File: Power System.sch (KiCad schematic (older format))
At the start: 19 parts

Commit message: changed the spliter simbole
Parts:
- removed U?: splitter, symbol splitter
- added U?: splitter, symbol splitter
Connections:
- wire segments 42 -> 44
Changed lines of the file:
@@
 	1323 4551 1848 4551
 Wire Wire Line
-	1853 4550 6700 4550
+	1853 4550 6900 4550
 Connection ~ 2400 4550
 Connection ~ 3100 4550
-$Comp
-L splitter U?
-U 1 1 59466E47
-P 1150 5075
-F 0 "U?" H 1150 4850 39  0000 C CNN
-F 1 "splitter" H 1150 5400 39  0000 C CNN
-F 2 "" H 1150 5075 39  0001 C CNN
-F 3 "" H 1150 5075 39  0001 C CNN
-	1    1150 5075
-	0    1    1    0
-$EndComp
 Wire Wire Line
 	1325 4550 1150 4550
@@
 	1    0    0    -1
 $EndComp
+$Comp
+L splitter U?
+U 1 1 594B2CCC
+P 1150 4875
+F 0 "U?" H 1190 4795 39  0000 C CNN
+F 1 "splitter" H 1180 4985 39  0000 C CNN
+F 2 "" H 1150 4875 39  0001 C CNN
+F 3 "" H 1150 4875 39  0001 C CNN
+	1    1150 4875
+	0    1    1    0
+$EndComp
+Wire Wire Line
+	1150 5375 1150 5075
+Wire Wire Line
+	7200 4550 7300 4550
 $EndSCHEMATC

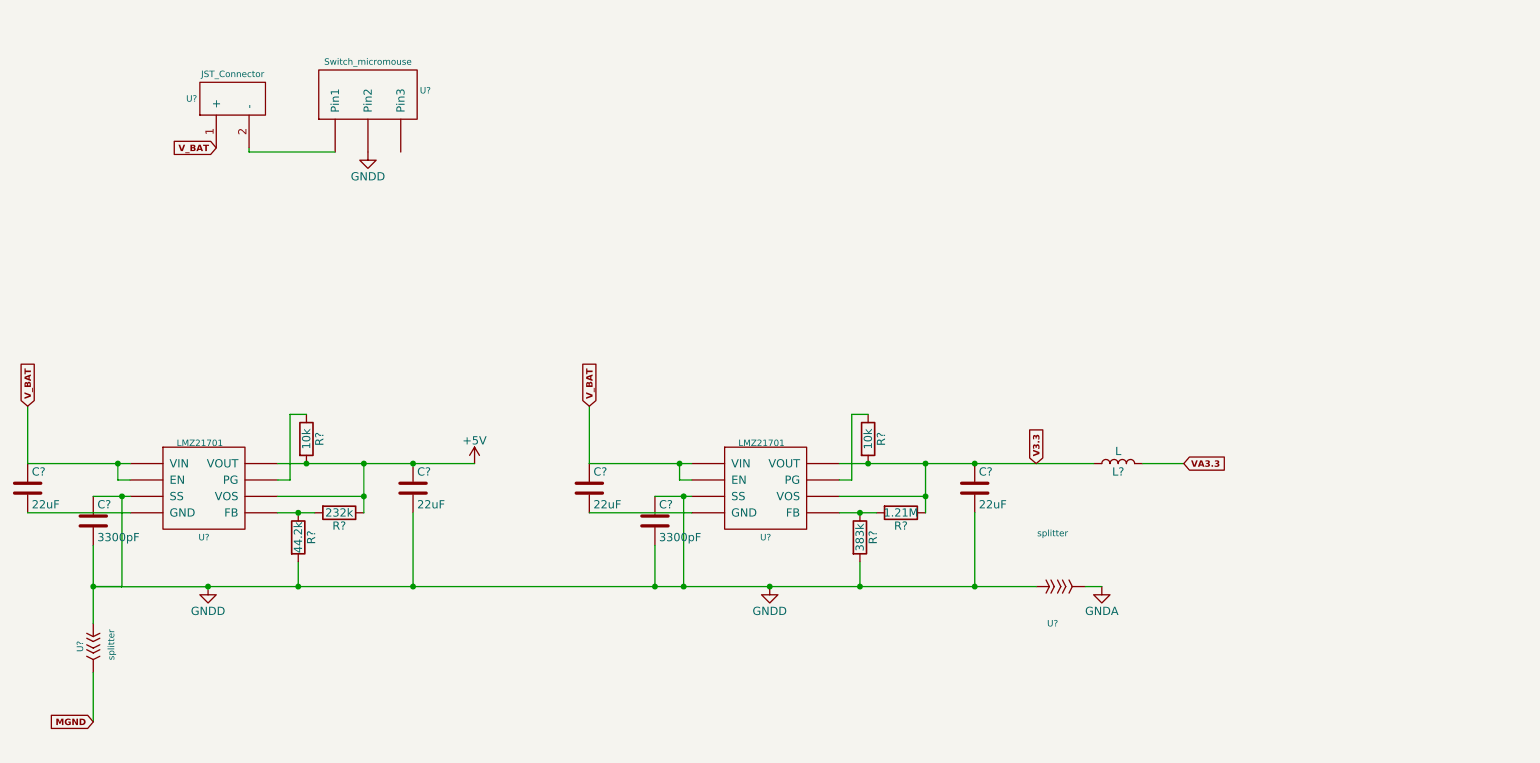
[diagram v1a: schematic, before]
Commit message: Created footprint for DC DC converter
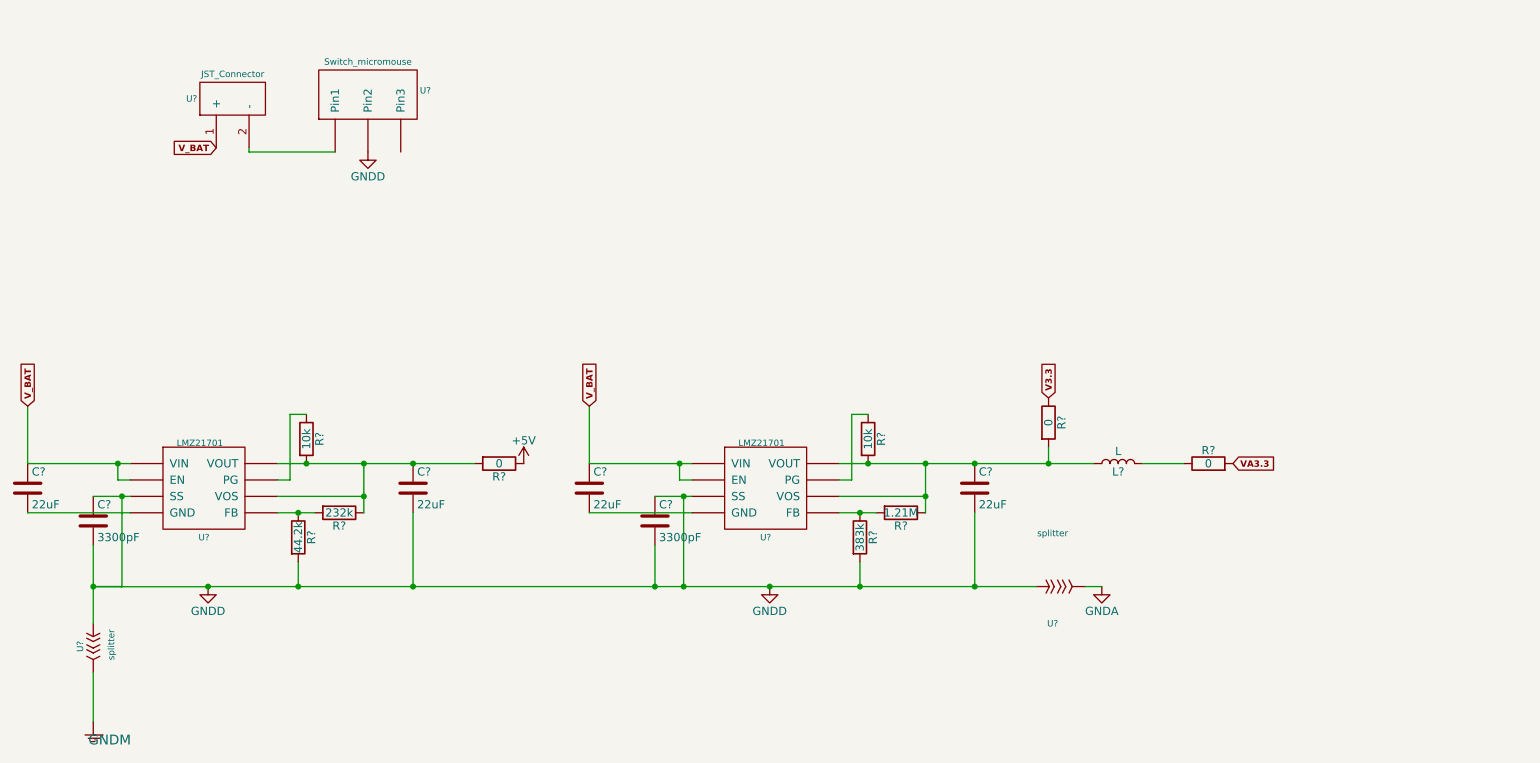
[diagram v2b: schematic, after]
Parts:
- added R? (x3): 0, symbol R
- added U?: GNDM, symbol GNDM
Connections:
- net labels removed: MGND
- wire segments 44 -> 45
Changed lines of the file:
@@
 Text GLabel 4175 3450 1    39   Input ~ 8
 V_BAT
-Text GLabel 6900 3800 1    39   Input ~ 8
+Text GLabel 6975 3400 1    39   Input ~ 8
 V3.3
 $Comp
@@
 	1325 4550 1150 4550
 Connection ~ 1150 4550
-Text GLabel 1150 5375 0    39   Input ~ 8
-MGND
 $Comp
 L GNDA #PWR?
@@
 L +5V #PWR?
 U 1 1 59467C95
-P 3475 3800
-F 0 "#PWR?" H 3475 3650 50  0001 C CNN
-F 1 "+5V" H 3475 3940 50  0000 C CNN
-F 2 "" H 3475 3800 50  0001 C CNN
-F 3 "" H 3475 3800 50  0001 C CNN
-	1    3475 3800
+P 3775 3800
+F 0 "#PWR?" H 3775 3650 50  0001 C CNN
+F 1 "+5V" H 3775 3940 50  0000 C CNN
+F 2 "" H 3775 3800 50  0001 C CNN
+F 3 "" H 3775 3800 50  0001 C CNN
+	1    3775 3800
 	1    0    0    -1
 $EndComp
@@
 Wire Wire Line
 	7550 3800 7800 3800
-Text GLabel 7800 3800 2    39   Input ~ 8
+Text GLabel 8100 3800 2    39   Input ~ 8
 VA3.3
 $Comp
@@
 Wire Wire Line
 	7200 4550 7300 4550
+$Comp
+L GNDM U?
+U 1 1 594B7C94
+P 1150 5475
+F 0 "U?" H 1250 5385 60  0001 C CNN
+F 1 "GNDM" H 1250 5465 60  0000 C CNN
+F 2 "" H 1150 5475 60  0001 C CNN
+F 3 "" H 1150 5475 60  0001 C CNN
+	1    1150 5475
+	1    0    0    -1
+$EndComp
+$Comp
+L R R?
+U 1 1 594B7E7A
+P 3625 3800
+F 0 "R?" V 3705 3800 50  0000 C CNN
+F 1 "0" V 3625 3800 50  0000 C CNN
+F 2 "" V 3555 3800 50  0001 C CNN
+F 3 "" H 3625 3800 50  0001 C CNN
+	1    3625 3800
+	0    1    1    0
+$EndComp
+$Comp
+L R R?
+U 1 1 594B8209
+P 6975 3550
+F 0 "R?" V 7055 3550 50  0000 C CNN
+F 1 "0" V 6975 3550 50  0000 C CNN
+F 2 "" V 6905 3550 50  0001 C CNN
+F 3 "" H 6975 3550 50  0001 C CNN
+	1    6975 3550
+	1    0    0    -1
+$EndComp
+Wire Wire Line
+	6975 3700 6975 3800
+Connection ~ 6975 3800
+$Comp
+L R R?
+U 1 1 594B84CE
+P 7950 3800
+F 0 "R?" V 8030 3800 50  0000 C CNN
+F 1 "0" V 7950 3800 50  0000 C CNN
+F 2 "" V 7880 3800 50  0001 C CNN
+F 3 "" H 7950 3800 50  0001 C CNN
+	1    7950 3800
+	0    -1   -1   0
+$EndComp
 $EndSCHEMATC

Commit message: created footprint for linear requlator
added footprint for microcontroller linear requlator
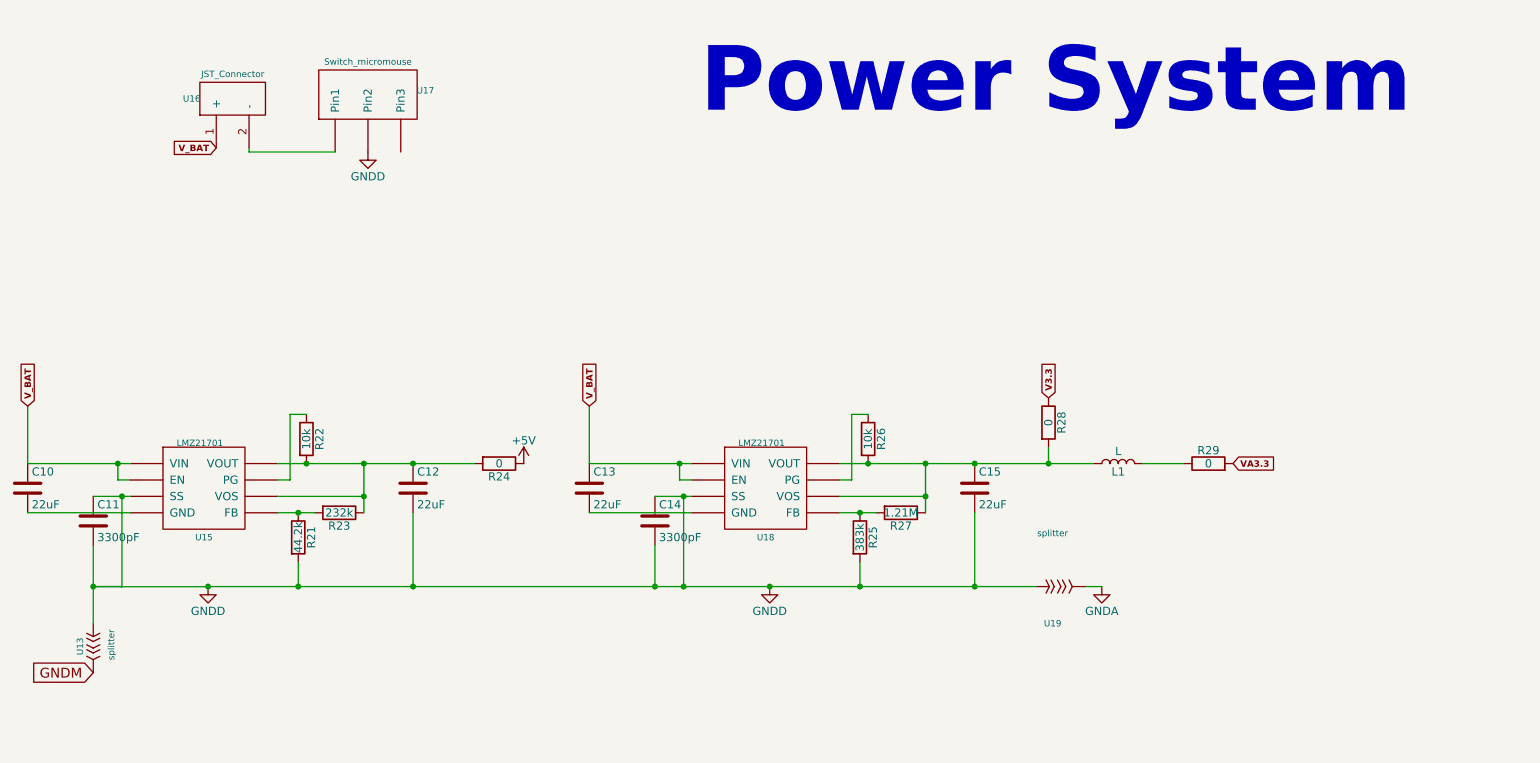
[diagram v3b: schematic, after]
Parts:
- removed U?: GNDM, symbol GNDM
- C10, C11, C12, C13, C14, C15: renamed from C?; footprint (none) -> Capacitors_SMD:C_0603
- L1: renamed from L?; footprint (none) -> Inductors_SMD:L_0603
- R21, R22, R23, R24, R25, R26, R27, R28, R29: renamed from R?; footprint (none) -> Resistors_SMD:R_0603
- U13: renamed from U?; footprint (none) -> micromouse:spliter
- U15, U18: renamed from U?; footprint (none) -> MicromouseFootprint:LMZ21701
- U17: renamed from U?; footprint (none) -> switch:CK-JS102011SAQN_sm-spdt-switch
- U19: renamed from U?; footprint (none) -> MicromouseFootprint:splitter
- gave numbers to parts that had none: 1
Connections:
- net labels added: GNDM
- wire segments 45 -> 44
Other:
- note added: "Power System"
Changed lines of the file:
@@
 $EndDescr
 $Comp
-L LMZ21701 U?
+L LMZ21701 U18
 U 1 1 59463C78
 P 5300 3900
-F 0 "U?" H 5250 3550 39  0000 C CNN
+F 0 "U18" H 5250 3550 39  0000 C CNN
 F 1 "LMZ21701" H 5225 4125 39  0000 C CNN
-F 2 "" H 5300 3600 39  0001 C CNN
+F 2 "MicromouseFootprint:LMZ21701" H 5300 3600 39  0001 C CNN
 F 3 "" H 5300 3600 39  0001 C CNN
 F 4 "LMZ21701SILT" H 5300 3500 39  0001 C CNN "manf#"
@@
 $EndComp
 $Comp
-L C C?
+L C C13
 U 1 1 59463D0A
 P 4175 3950
-F 0 "C?" H 4200 4050 50  0000 L CNN
+F 0 "C13" H 4200 4050 50  0000 L CNN
 F 1 "22uF" H 4200 3850 50  0000 L CNN
-F 2 "" H 4213 3800 50  0001 C CNN
+F 2 "Capacitors_SMD:C_0603" H 4213 3800 50  0001 C CNN
 F 3 "" H 4175 3950 50  0001 C CNN
 	1    4175 3950
@@
 $EndComp
 $Comp
-L C C?
+L C C14
 U 1 1 59463D30
 P 4575 4150
-F 0 "C?" H 4600 4250 50  0000 L CNN
+F 0 "C14" H 4600 4250 50  0000 L CNN
 F 1 "3300pF" H 4600 4050 50  0000 L CNN
-F 2 "" H 4613 4000 50  0001 C CNN
+F 2 "Capacitors_SMD:C_0603" H 4613 4000 50  0001 C CNN
 F 3 "" H 4575 4150 50  0001 C CNN
 	1    4575 4150
@@
 $EndComp
 $Comp
-L C C?
+L C C15
 U 1 1 59463D56
 P 6525 3950
-F 0 "C?" H 6550 4050 50  0000 L CNN
+F 0 "C15" H 6550 4050 50  0000 L CNN
 F 1 "22uF" H 6550 3850 50  0000 L CNN
-F 2 "" H 6563 3800 50  0001 C CNN
+F 2 "Capacitors_SMD:C_0603" H 6563 3800 50  0001 C CNN
 F 3 "" H 6525 3950 50  0001 C CNN
 	1    6525 3950
@@
 $EndComp
 $Comp
-L R R?
+L R R27
 U 1 1 59463EA4
 P 6075 4100
-F 0 "R?" V 6155 4100 50  0000 C CNN
+F 0 "R27" V 6155 4100 50  0000 C CNN
 F 1 "1.21M" V 6075 4100 50  0000 C CNN
-F 2 "" V 6005 4100 50  0001 C CNN
+F 2 "Resistors_SMD:R_0603" V 6005 4100 50  0001 C CNN
 F 3 "" H 6075 4100 50  0001 C CNN
 	1    6075 4100
@@
 $EndComp
 $Comp
-L R R?
+L R R25
 U 1 1 59463ED5
 P 5825 4250
-F 0 "R?" V 5905 4250 50  0000 C CNN
+F 0 "R25" V 5905 4250 50  0000 C CNN
 F 1 "383k" V 5825 4250 50  0000 C CNN
-F 2 "" V 5755 4250 50  0001 C CNN
+F 2 "Resistors_SMD:R_0603" V 5755 4250 50  0001 C CNN
 F 3 "" H 5825 4250 50  0001 C CNN
 	1    5825 4250
@@
 $EndComp
 $Comp
-L GNDD #PWR?
+L GNDD #PWR010
 U 1 1 59463FDA
 P 5275 4550
-F 0 "#PWR?" H 5275 4300 50  0001 C CNN
+F 0 "#PWR010" H 5275 4300 50  0001 C CNN
 F 1 "GNDD" H 5275 4400 50  0000 C CNN
 F 2 "" H 5275 4550 50  0001 C CNN
@@
 $EndComp
 $Comp
-L R R?
+L R R26
 U 1 1 594642FB
 P 5875 3650
-F 0 "R?" V 5955 3650 50  0000 C CNN
+F 0 "R26" V 5955 3650 50  0000 C CNN
 F 1 "10k" V 5875 3650 50  0000 C CNN
-F 2 "" V 5805 3650 50  0001 C CNN
+F 2 "Resistors_SMD:R_0603" V 5805 3650 50  0001 C CNN
 F 3 "" H 5875 3650 50  0001 C CNN
 	1    5875 3650
@@
 V3.3
 $Comp
-L splitter U?
+L splitter U19
 U 1 1 5946550D
 P 7000 4550
-F 0 "U?" H 7000 4325 39  0000 C CNN
+F 0 "U19" H 7000 4325 39  0000 C CNN
 F 1 "splitter" H 7000 4875 39  0000 C CNN
-F 2 "" H 7000 4550 39  0001 C CNN
+F 2 "MicromouseFootprint:splitter" H 7000 4550 39  0001 C CNN
 F 3 "" H 7000 4550 39  0001 C CNN
 	1    7000 4550
@@
 $EndComp
 $Comp
-L LMZ21701 U?
+L LMZ21701 U15
 U 1 1 59465F6A
 P 1875 3900
-F 0 "U?" H 1825 3550 39  0000 C CNN
+F 0 "U15" H 1825 3550 39  0000 C CNN
 F 1 "LMZ21701" H 1800 4125 39  0000 C CNN
-F 2 "" H 1875 3600 39  0001 C CNN
+F 2 "MicromouseFootprint:LMZ21701" H 1875 3600 39  0001 C CNN
 F 3 "" H 1875 3600 39  0001 C CNN
 F 4 "LMZ21701SILT" H 1875 3500 39  0001 C CNN "manf#"
@@
 $EndComp
 $Comp
-L C C?
+L C C10
 U 1 1 59465F70
 P 750 3950
-F 0 "C?" H 775 4050 50  0000 L CNN
+F 0 "C10" H 775 4050 50  0000 L CNN
 F 1 "22uF" H 775 3850 50  0000 L CNN
-F 2 "" H 788 3800 50  0001 C CNN
+F 2 "Capacitors_SMD:C_0603" H 788 3800 50  0001 C CNN
 F 3 "" H 750 3950 50  0001 C CNN
 	1    750  3950
@@
 $EndComp
 $Comp
-L C C?
+L C C11
 U 1 1 59465F76
 P 1150 4150
-F 0 "C?" H 1175 4250 50  0000 L CNN
+F 0 "C11" H 1175 4250 50  0000 L CNN
 F 1 "3300pF" H 1175 4050 50  0000 L CNN
-F 2 "" H 1188 4000 50  0001 C CNN
+F 2 "Capacitors_SMD:C_0603" H 1188 4000 50  0001 C CNN
 F 3 "" H 1150 4150 50  0001 C CNN
 	1    1150 4150
@@
 $EndComp
 $Comp
-L C C?
+L C C12
 U 1 1 59465F7C
 P 3100 3950
-F 0 "C?" H 3125 4050 50  0000 L CNN
+F 0 "C12" H 3125 4050 50  0000 L CNN
 F 1 "22uF" H 3125 3850 50  0000 L CNN
-F 2 "" H 3138 3800 50  0001 C CNN
+F 2 "Capacitors_SMD:C_0603" H 3138 3800 50  0001 C CNN
 F 3 "" H 3100 3950 50  0001 C CNN
 	1    3100 3950
@@
 $EndComp
 $Comp
-L R R?
+L R R23
 U 1 1 59465F84
 P 2650 4100
-F 0 "R?" V 2730 4100 50  0000 C CNN
+F 0 "R23" V 2730 4100 50  0000 C CNN
 F 1 "232k" V 2650 4100 50  0000 C CNN
-F 2 "" V 2580 4100 50  0001 C CNN
+F 2 "Resistors_SMD:R_0603" V 2580 4100 50  0001 C CNN
 F 3 "" H 2650 4100 50  0001 C CNN
 	1    2650 4100
@@
 $EndComp
 $Comp
-L R R?
+L R R21
 U 1 1 59465F8A
 P 2400 4250
-F 0 "R?" V 2480 4250 50  0000 C CNN
+F 0 "R21" V 2480 4250 50  0000 C CNN
 F 1 "44.2k" V 2400 4250 50  0000 C CNN
-F 2 "" V 2330 4250 50  0001 C CNN
+F 2 "Resistors_SMD:R_0603" V 2330 4250 50  0001 C CNN
 F 3 "" H 2400 4250 50  0001 C CNN
 	1    2400 4250
@@
 $EndComp
 $Comp
-L GNDD #PWR?
+L GNDD #PWR011
 U 1 1 59465F90
 P 1850 4550
-F 0 "#PWR?" H 1850 4300 50  0001 C CNN
+F 0 "#PWR011" H 1850 4300 50  0001 C CNN
 F 1 "GNDD" H 1850 4400 50  0000 C CNN
 F 2 "" H 1850 4550 50  0001 C CNN
@@
 $EndComp
 $Comp
-L R R?
+L R R22
 U 1 1 59465F96
 P 2450 3650
-F 0 "R?" V 2530 3650 50  0000 C CNN
+F 0 "R22" V 2530 3650 50  0000 C CNN
 F 1 "10k" V 2450 3650 50  0000 C CNN
-F 2 "" V 2380 3650 50  0001 C CNN
+F 2 "Resistors_SMD:R_0603" V 2380 3650 50  0001 C CNN
 F 3 "" H 2450 3650 50  0001 C CNN
 	1    2450 3650
@@
 Connection ~ 1150 4550
 $Comp
-L GNDA #PWR?
+L GNDA #PWR012
 U 1 1 594675FB
 P 7300 4550
-F 0 "#PWR?" H 7300 4300 50  0001 C CNN
+F 0 "#PWR012" H 7300 4300 50  0001 C CNN
 F 1 "GNDA" H 7300 4400 50  0000 C CNN
 F 2 "" H 7300 4550 50  0001 C CNN
@@
 $EndComp
 $Comp
-L +5V #PWR?
+L +5V #PWR013
 U 1 1 59467C95
 P 3775 3800
-F 0 "#PWR?" H 3775 3650 50  0001 C CNN
+F 0 "#PWR013" H 3775 3650 50  0001 C CNN
 F 1 "+5V" H 3775 3940 50  0000 C CNN
 F 2 "" H 3775 3800 50  0001 C CNN
@@
 $EndComp
 $Comp
-L L L?
+L L L1
 U 1 1 59467F19
 P 7400 3800
-F 0 "L?" V 7350 3800 50  0000 C CNN
+F 0 "L1" V 7350 3800 50  0000 C CNN
 F 1 "L" V 7475 3800 50  0000 C CNN
-F 2 "" H 7400 3800 50  0001 C CNN
+F 2 "Inductors_SMD:L_0603" H 7400 3800 50  0001 C CNN
 F 3 "" H 7400 3800 50  0001 C CNN
 	1    7400 3800
@@
 VA3.3
 $Comp
-L JST_Connector U?
+L JST_Connector U16
 U 1 1 594682BF
 P 2000 1675
-F 0 "U?" H 1750 1775 39  0000 C CNN
+F 0 "U16" H 1750 1775 39  0000 C CNN
 F 1 "JST_Connector" H 2000 1925 39  0000 C CNN
 F 2 "" H 2000 1675 39  0001 C CNN
@@
 $EndComp
 $Comp
-L Switch_micromouse U?
+L Switch_micromouse U17
 U 1 1 59468311
 P 2925 1700
-F 0 "U?" H 3175 1875 39  0000 C CNN
+F 0 "U17" H 3175 1875 39  0000 C CNN
 F 1 "Switch_micromouse" H 2825 2050 39  0000 C CNN
-F 2 "" H 2925 1700 39  0001 C CNN
+F 2 "switch:CK-JS102011SAQN_sm-spdt-switch" H 2925 1700 39  0001 C CNN
 F 3 "" H 2925 1700 39  0001 C CNN
 	1    2925 1700
@@
 V_BAT
 $Comp
-L GNDD #PWR?
+L GNDD #PWR014
 U 1 1 59468675
 P 2825 1900
-F 0 "#PWR?" H 2825 1650 50  0001 C CNN
+F 0 "#PWR014" H 2825 1650 50  0001 C CNN
 F 1 "GNDD" H 2825 1750 50  0000 C CNN
 F 2 "" H 2825 1900 50  0001 C CNN
@@
 $EndComp
 $Comp
-L splitter U?
+L splitter U13
 U 1 1 594B2CCC
 P 1150 4875
-F 0 "U?" H 1190 4795 39  0000 C CNN
+F 0 "U13" H 1190 4795 39  0000 C CNN
 F 1 "splitter" H 1180 4985 39  0000 C CNN
-F 2 "" H 1150 4875 39  0001 C CNN
+F 2 "micromouse:spliter" H 1150 4875 39  0001 C CNN
 F 3 "" H 1150 4875 39  0001 C CNN
 	1    1150 4875
@@
 $EndComp
 Wire Wire Line
-	1150 5375 1150 5075
-Wire Wire Line
 	7200 4550 7300 4550
 $Comp
-L GNDM U?
-U 1 1 594B7C94
-P 1150 5475
-F 0 "U?" H 1250 5385 60  0001 C CNN
-F 1 "GNDM" H 1250 5465 60  0000 C CNN
-F 2 "" H 1150 5475 60  0001 C CNN
-F 3 "" H 1150 5475 60  0001 C CNN
-	1    1150 5475
-	1    0    0    -1
-$EndComp
-$Comp
-L R R?
+L R R24
 U 1 1 594B7E7A
 P 3625 3800
-F 0 "R?" V 3705 3800 50  0000 C CNN
+F 0 "R24" V 3705 3800 50  0000 C CNN
 F 1 "0" V 3625 3800 50  0000 C CNN
-F 2 "" V 3555 3800 50  0001 C CNN
+F 2 "Resistors_SMD:R_0603" V 3555 3800 50  0001 C CNN
 F 3 "" H 3625 3800 50  0001 C CNN
 	1    3625 3800
@@
 $EndComp
 $Comp
-L R R?
+L R R28
 U 1 1 594B8209
 P 6975 3550
-F 0 "R?" V 7055 3550 50  0000 C CNN
+F 0 "R28" V 7055 3550 50  0000 C CNN
 F 1 "0" V 6975 3550 50  0000 C CNN
-F 2 "" V 6905 3550 50  0001 C CNN
+F 2 "Resistors_SMD:R_0603" V 6905 3550 50  0001 C CNN
 F 3 "" H 6975 3550 50  0001 C CNN
 	1    6975 3550
@@
 Connection ~ 6975 3800
 $Comp
-L R R?
+L R R29
 U 1 1 594B84CE
 P 7950 3800
-F 0 "R?" V 8030 3800 50  0000 C CNN
+F 0 "R29" V 8030 3800 50  0000 C CNN
 F 1 "0" V 7950 3800 50  0000 C CNN
-F 2 "" V 7880 3800 50  0001 C CNN
+F 2 "Resistors_SMD:R_0603" V 7880 3800 50  0001 C CNN
 F 3 "" H 7950 3800 50  0001 C CNN
 	1    7950 3800
 	0    -1   -1   0
 $EndComp
+Text Notes 4850 1700 0    394  ~ 79
+Power System
+Text GLabel 1150 5075 0    60   Input ~ 0
+GNDM
 $EndSCHEMATC
